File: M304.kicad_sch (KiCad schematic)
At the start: 89 parts, among them J1 LCD 2004, J2 Relay OUT, J3 iM920, J4 GPS, J5 Conn_01x02, P1 Digital, P10 CONN_01X01, P11 CONN_01X01, P12 CONN_01X01, P13 CONN_01X01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

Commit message: 大修正
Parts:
- removed JA15: Conn_01x03, Connector_JST:JST_XH_B3B-XH-A_1x03_P2.50mm_Vertical, symbol Connector_Generic:Conn_01x03
- added RV2: B10k, Potentiometer_THT:Potentiometer_Alps_RK09K_Single_Vertical, symbol Device:R_Potentiometer_MountingPin
- C1, C2: footprint (none) -> Capacitor_THT:C_Disc_D3.0mm_W2.0mm_P2.50mm
- C3: value 100u/35V -> 100u/25V; footprint (none) -> Capacitor_THT:CP_Radial_D5.0mm_P2.00mm
- J5: footprint (none) -> Connector_JST:JST_VH_B2P-VH_1x02_P3.96mm_Vertical
- R1, R2, R3, R4, R5, R6: footprint (none) -> Resistor_THT:R_Axial_DIN0207_L6.3mm_D2.5mm_P7.62mm_Horizontal
- RV1: value 10k -> B10k
- SW1, SW2, SW3, SW4, SW5: footprint (none) -> HOLLY:TVDT18-050
- U1: footprint Package_DIP:DIP-8_W7.62mm -> Package_DIP:DIP-8_W7.62mm_LongPads
- Y1: footprint (none) -> Crystal:Crystal_C26-LF_D2.1mm_L6.5mm_Horizontal
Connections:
- net +5V: now also RV1.3, RV2.3; no longer RV1.1
- net A15: now also RV2.2
- net GND: now also RV1.1, RV2.1, RV2.MP (MountPin); no longer RV1.3
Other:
- note added: "P-14827"

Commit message: PCB layout
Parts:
- removed JD32: Conn_01x01, Connector_Pin:Pin_D0.9mm_L10.0mm_W2.4mm_FlatFork, symbol Connector_Generic:Conn_01x01
- added SW6: SW_ENTER, HOLLY:TVDT18-050, symbol Switch:SW_SPST
- J1: footprint Connector_PinHeader_2.54mm:PinHeader_1x16_P2.54mm_Vertical -> Connector_PinSocket_2.54mm:PinSocket_1x16_P2.54mm_Vertical
- P2: footprint Socket_Arduino_Mega:Socket_Strip_Arduino_1x08 -> Connector_PinHeader_2.54mm:PinHeader_1x08_P2.54mm_Vertical
- renumbered SW6 to SW7
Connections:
- net 32: now also SW6.2 (B)
- net GND: now also SW6.1 (A)
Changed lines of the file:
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@@
     (stroke (width 0) (type default) (color 0 0 0 0))
   )
+  (wire (pts (xy 165.1 161.29) (xy 165.1 165.1))
+    (stroke (width 0) (type default) (color 0 0 0 0))
+  )
   (wire (pts (xy 30.48 124.46) (xy 36.83 124.46))
     (stroke (width 0) (type default) (color 0 0 0 0))
   )
+  (wire (pts (xy 167.64 176.53) (xy 167.64 179.07))
+    (stroke (width 0) (type default) (color 0 0 0 0))
+  )
   (wire (pts (xy 149.86 120.65) (xy 149.86 135.89))
     (stroke (width 0) (type default) (color 0 0 0 0))
@@
     (stroke (width 0) (type default) (color 0 0 0 0))
   )
+  (wire (pts (xy 167.64 165.1) (xy 167.64 166.37))
+    (stroke (width 0) (type default) (color 0 0 0 0))
+  )
   (wire (pts (xy 156.21 72.39) (xy 179.07 72.39))
     (stroke (width 0) (type solid) (color 0 0 0 0))
@@
     (stroke (width 0) (type default) (color 0 0 0 0))
   )
+  (wire (pts (xy 165.1 165.1) (xy 167.64 165.1))
+    (stroke (width 0) (type default) (color 0 0 0 0))
+  )
   (wire (pts (xy 39.37 127) (xy 39.37 138.43))
     (stroke (width 0) (type default) (color 0 0 0 0))
@@
     (stroke (width 0) (type default) (color 0 0 0 0))
   )
-  (wire (pts (xy 146.05 161.29) (xy 151.13 161.29))
-    (stroke (width 0) (type solid) (color 0 0 0 0))
-  )
   (wire (pts (xy 177.8 162.56) (xy 194.31 162.56))
     (stroke (width 0) (type default) (color 0 0 0 0))
@@
     (stroke (width 0) (type default) (color 0 0 0 0))
   )
+  (wire (pts (xy 146.05 161.29) (xy 165.1 161.29))
+    (stroke (width 0) (type default) (color 0 0 0 0))
+  )
   (wire (pts (xy 209.55 149.86) (xy 209.55 142.24))
     (stroke (width 0) (type default) (color 0 0 0 0))
@@
     (property "Reference" "P2" (id 0) (at 140.97 41.91 0))
     (property "Value" "Power" (id 1) (at 143.51 52.07 90))
-    (property "Footprint" "Socket_Arduino_Mega:Socket_Strip_Arduino_1x08" (id 2) (at 140.97 52.07 0)
+    (property "Footprint" "Connector_PinHeader_2.54mm:PinHeader_1x08_P2.54mm_Vertical" (id 2) (at 140.97 52.07 0)
       (effects (font (size 1.27 1.27)) hide)
     )
@@
       (effects (font (size 1.27 1.27)) (justify left))
     )
-    (property "Footprint" "Connector_PinHeader_2.54mm:PinHeader_1x16_P2.54mm_Vertical" (id 2) (at 224.79 142.24 0)
+    (property "Footprint" "Connector_PinSocket_2.54mm:PinSocket_1x16_P2.54mm_Vertical" (id 2) (at 224.79 142.24 0)
       (effects (font (size 1.27 1.27)) hide)
     )
@@
     (pin "3")
   )
+  (symbol (lib_id "power:GND") (at 167.64 179.07 0) (unit 1)
+    (in_bom yes) (on_board yes)
+    (property "Reference" "#PWR0138" (id 0) (at 167.64 185.42 0)
+      (effects (font (size 1.27 1.27)) hide)
+    )
+    (property "Value" "GND" (id 1) (at 167.64 184.15 90)
+      (effects (font (size 1 1)))
+    )
+    (property "Footprint" "" (id 2) (at 167.64 179.07 0))
+    (property "Datasheet" "" (id 3) (at 167.64 179.07 0))
+    (pin "1")
+  )
   (symbol (lib_id "power:GND") (at 269.24 50.8 0) (unit 1)
     (in_bom yes) (on_board yes)
@@
   (symbol (lib_id "Switch:SW_SPST") (at 193.802 82.55 0) (mirror y) (unit 1)
     (in_bom yes) (on_board yes)
-    (property "Reference" "SW6" (id 0) (at 189.992 81.28 0)
+    (property "Reference" "SW7" (id 0) (at 189.992 81.28 0)
       (effects (font (size 1 1)))
     )
@@
     (pin "2")
   )
-  (symbol (lib_id "Connector_Generic:Conn_01x01") (at 156.21 161.29 0) (unit 1)
-    (in_bom yes) (on_board yes)
-    (property "Reference" "JD32" (id 0) (at 158.75 161.29 0)
-      (effects (font (size 1.27 1.27)) (justify left))
-    )
-    (property "Value" "Conn_01x01" (id 1) (at 158.242 162.9922 0)
-      (effects (font (size 1.27 1.27)) (justify left) hide)
-    )
-    (property "Footprint" "Connector_Pin:Pin_D0.9mm_L10.0mm_W2.4mm_FlatFork" (id 2) (at 156.21 161.29 0)
-      (effects (font (size 1.27 1.27)) hide)
-    )
-    (property "Datasheet" "~" (id 3) (at 156.21 161.29 0)
-      (effects (font (size 1.27 1.27)) hide)
-    )
-    (pin "1")
-  )
   (symbol (lib_id "Connector_Generic:Conn_01x02") (at 260.35 36.83 0) (unit 1)
     (in_bom yes) (on_board yes)
@@
     (pin "5")
   )
+  (symbol (lib_id "Switch:SW_SPST") (at 167.64 171.45 270) (mirror x) (unit 1)
+    (in_bom yes) (on_board yes)
+    (property "Reference" "SW6" (id 0) (at 165.1 171.45 90)
+      (effects (font (size 1 1)))
+    )
+    (property "Value" "SW_ENTER" (id 1) (at 172.72 172.72 90)
+      (effects (font (size 1 1)))
+    )
+    (property "Footprint" "HOLLY:TVDT18-050" (id 2) (at 167.64 171.45 0)
+      (effects (font (size 1.27 1.27)) hide)
+    )
+    (property "Datasheet" "~" (id 3) (at 167.64 171.45 0)
+      (effects (font (size 1.27 1.27)) hide)
+    )
+    (pin "1")
+    (pin "2")
+  )
   (symbol (lib_id "power:GND") (at 82.55 35.56 0) (unit 1)
     (in_bom yes) (on_board yes)
@@
       (reference "#PWR0137") (unit 1) (value "GND") (footprint "")
     )
+    (path "/3a7afde4-db0a-4309-bece-1305421c4024"
+      (reference "#PWR0138") (unit 1) (value "GND") (footprint "")
+    )
     (path "/7629fb6d-20db-4e52-aca9-1faafbccf85c"
       (reference "BT1") (unit 1) (value "CR2032") (footprint "")
@@
     )
     (path "/2812c426-eaaa-40f0-875f-9c01c02e0a76"
-      (reference "J1") (unit 1) (value "LCD 2004") (footprint "Connector_PinHeader_2.54mm:PinHeader_1x16_P2.54mm_Vertical")
+      (reference "J1") (unit 1) (value "LCD 2004") (footprint "Connector_PinSocket_2.54mm:PinSocket_1x16_P2.54mm_Vertical")
     )
     (path "/cf4a0d7b-49d0-4fab-a66e-8cf646496452"
@@
       (reference "JD31") (unit 1) (value "Conn_01x01") (footprint "Connector_Pin:Pin_D0.9mm_L10.0mm_W2.4mm_FlatFork")
     )
-    (path "/9eb5f420-8ac2-4cff-9412-80ef6b7747c6"
-      (reference "JD32") (unit 1) (value "Conn_01x01") (footprint "Connector_Pin:Pin_D0.9mm_L10.0mm_W2.4mm_FlatFork")
-    )
     (path "/b0e37c59-828f-45f4-9524-3ceeeb2c5150"
       (reference "JD48") (unit 1) (value "Conn_01x01") (footprint "Connector_Pin:Pin_D0.9mm_L10.0mm_W2.4mm_FlatFork")
@@
     )
     (path "/00000000-0000-0000-0000-000056d71773"
-      (reference "P2") (unit 1) (value "Power") (footprint "Socket_Arduino_Mega:Socket_Strip_Arduino_1x08")
+      (reference "P2") (unit 1) (value "Power") (footprint "Connector_PinHeader_2.54mm:PinHeader_1x08_P2.54mm_Vertical")
     )
     (path "/00000000-0000-0000-0000-000056d72f1c"
@@
       (reference "SW5") (unit 1) (value "SW_D") (footprint "HOLLY:TVDT18-050")
     )
+    (path "/eab964a3-3b27-437e-9f6c-be163cd40f3e"
+      (reference "SW6") (unit 1) (value "SW_ENTER") (footprint "HOLLY:TVDT18-050")
+    )
     (path "/70315b01-1acb-4620-a09c-cc62e59d80b5"
-      (reference "SW6") (unit 1) (value "SAFEMODE") (footprint "")
+      (reference "SW7") (unit 1) (value "SAFEMODE") (footprint "")
     )
     (path "/2da95ce6-0997-43ec-959b-0f1144d39cac"

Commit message: Arduino MEGA pin direction change
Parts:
- P1: footprint Socket_Arduino_Mega:Socket_Strip_Arduino_2x18 -> Connector_PinHeader_2.54mm:PinHeader_2x18_P2.54mm_Vertical
- P3, P4, P6, P7: footprint Socket_Arduino_Mega:Socket_Strip_Arduino_1x08 -> Connector_PinHeader_2.54mm:PinHeader_1x08_P2.54mm_Vertical
- P5: footprint Socket_Arduino_Mega:Socket_Strip_Arduino_1x10 -> Connector_PinHeader_2.54mm:PinHeader_1x10_P2.54mm_Vertical
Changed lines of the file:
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@@
     (property "Reference" "P5" (id 0) (at 151.13 36.83 0))
     (property "Value" "PWM" (id 1) (at 148.59 49.53 90))
-    (property "Footprint" "Socket_Arduino_Mega:Socket_Strip_Arduino_1x10" (id 2) (at 151.13 49.53 0)
+    (property "Footprint" "Connector_PinHeader_2.54mm:PinHeader_1x10_P2.54mm_Vertical" (id 2) (at 151.13 49.53 0)
       (effects (font (size 1.27 1.27)) hide)
     )
@@
     (property "Reference" "P3" (id 0) (at 140.97 69.85 0))
     (property "Value" "Analog" (id 1) (at 143.51 80.01 90))
-    (property "Footprint" "Socket_Arduino_Mega:Socket_Strip_Arduino_1x08" (id 2) (at 140.97 80.01 0)
+    (property "Footprint" "Connector_PinHeader_2.54mm:PinHeader_1x08_P2.54mm_Vertical" (id 2) (at 140.97 80.01 0)
       (effects (font (size 1.27 1.27)) hide)
     )
@@
     (property "Reference" "P6" (id 0) (at 151.13 69.85 0))
     (property "Value" "PWM" (id 1) (at 148.59 80.01 90))
-    (property "Footprint" "Socket_Arduino_Mega:Socket_Strip_Arduino_1x08" (id 2) (at 151.13 80.01 0)
+    (property "Footprint" "Connector_PinHeader_2.54mm:PinHeader_1x08_P2.54mm_Vertical" (id 2) (at 151.13 80.01 0)
       (effects (font (size 1.27 1.27)) hide)
     )
@@
     (property "Reference" "P4" (id 0) (at 140.97 93.98 0))
     (property "Value" "Analog" (id 1) (at 143.51 104.14 90))
-    (property "Footprint" "Socket_Arduino_Mega:Socket_Strip_Arduino_1x08" (id 2) (at 140.97 104.14 0)
+    (property "Footprint" "Connector_PinHeader_2.54mm:PinHeader_1x08_P2.54mm_Vertical" (id 2) (at 140.97 104.14 0)
       (effects (font (size 1.27 1.27)) hide)
     )
@@
     (property "Reference" "P7" (id 0) (at 151.13 93.98 0))
     (property "Value" "Communication" (id 1) (at 148.59 104.14 90))
-    (property "Footprint" "Socket_Arduino_Mega:Socket_Strip_Arduino_1x08" (id 2) (at 151.13 104.14 0)
+    (property "Footprint" "Connector_PinHeader_2.54mm:PinHeader_1x08_P2.54mm_Vertical" (id 2) (at 151.13 104.14 0)
       (effects (font (size 1.27 1.27)) hide)
     )
@@
     (property "Reference" "P1" (id 0) (at 140.97 129.54 0))
     (property "Value" "Digital" (id 1) (at 140.97 153.67 90))
-    (property "Footprint" "Socket_Arduino_Mega:Socket_Strip_Arduino_2x18" (id 2) (at 140.97 180.34 0)
+    (property "Footprint" "Connector_PinHeader_2.54mm:PinHeader_2x18_P2.54mm_Vertical" (id 2) (at 140.97 180.34 0)
       (effects (font (size 1.27 1.27)) hide)
     )
@@
     )
     (path "/00000000-0000-0000-0000-000056d743b5"
-      (reference "P1") (unit 1) (value "Digital") (footprint "Socket_Arduino_Mega:Socket_Strip_Arduino_2x18")
+      (reference "P1") (unit 1) (value "Digital") (footprint "Connector_PinHeader_2.54mm:PinHeader_2x18_P2.54mm_Vertical")
     )
     (path "/00000000-0000-0000-0000-000056d71773"
@@
     )
     (path "/00000000-0000-0000-0000-000056d72f1c"
-      (reference "P3") (unit 1) (value "Analog") (footprint "Socket_Arduino_Mega:Socket_Strip_Arduino_1x08")
+      (reference "P3") (unit 1) (value "Analog") (footprint "Connector_PinHeader_2.54mm:PinHeader_1x08_P2.54mm_Vertical")
     )
     (path "/00000000-0000-0000-0000-000056d73a0e"
-      (reference "P4") (unit 1) (value "Analog") (footprint "Socket_Arduino_Mega:Socket_Strip_Arduino_1x08")
+      (reference "P4") (unit 1) (value "Analog") (footprint "Connector_PinHeader_2.54mm:PinHeader_1x08_P2.54mm_Vertical")
     )
     (path "/00000000-0000-0000-0000-000056d72368"
-      (reference "P5") (unit 1) (value "PWM") (footprint "Socket_Arduino_Mega:Socket_Strip_Arduino_1x10")
+      (reference "P5") (unit 1) (value "PWM") (footprint "Connector_PinHeader_2.54mm:PinHeader_1x10_P2.54mm_Vertical")
     )
     (path "/00000000-0000-0000-0000-000056d734d0"
-      (reference "P6") (unit 1) (value "PWM") (footprint "Socket_Arduino_Mega:Socket_Strip_Arduino_1x08")
+      (reference "P6") (unit 1) (value "PWM") (footprint "Connector_PinHeader_2.54mm:PinHeader_1x08_P2.54mm_Vertical")
     )
     (path "/00000000-0000-0000-0000-000056d73f2c"
-      (reference "P7") (unit 1) (value "Communication") (footprint "Socket_Arduino_Mega:Socket_Strip_Arduino_1x08")
+      (reference "P7") (unit 1) (value "Communication") (footprint "Connector_PinHeader_2.54mm:PinHeader_1x08_P2.54mm_Vertical")
     )
     (path "/00000000-0000-0000-0000-000056d70b71"

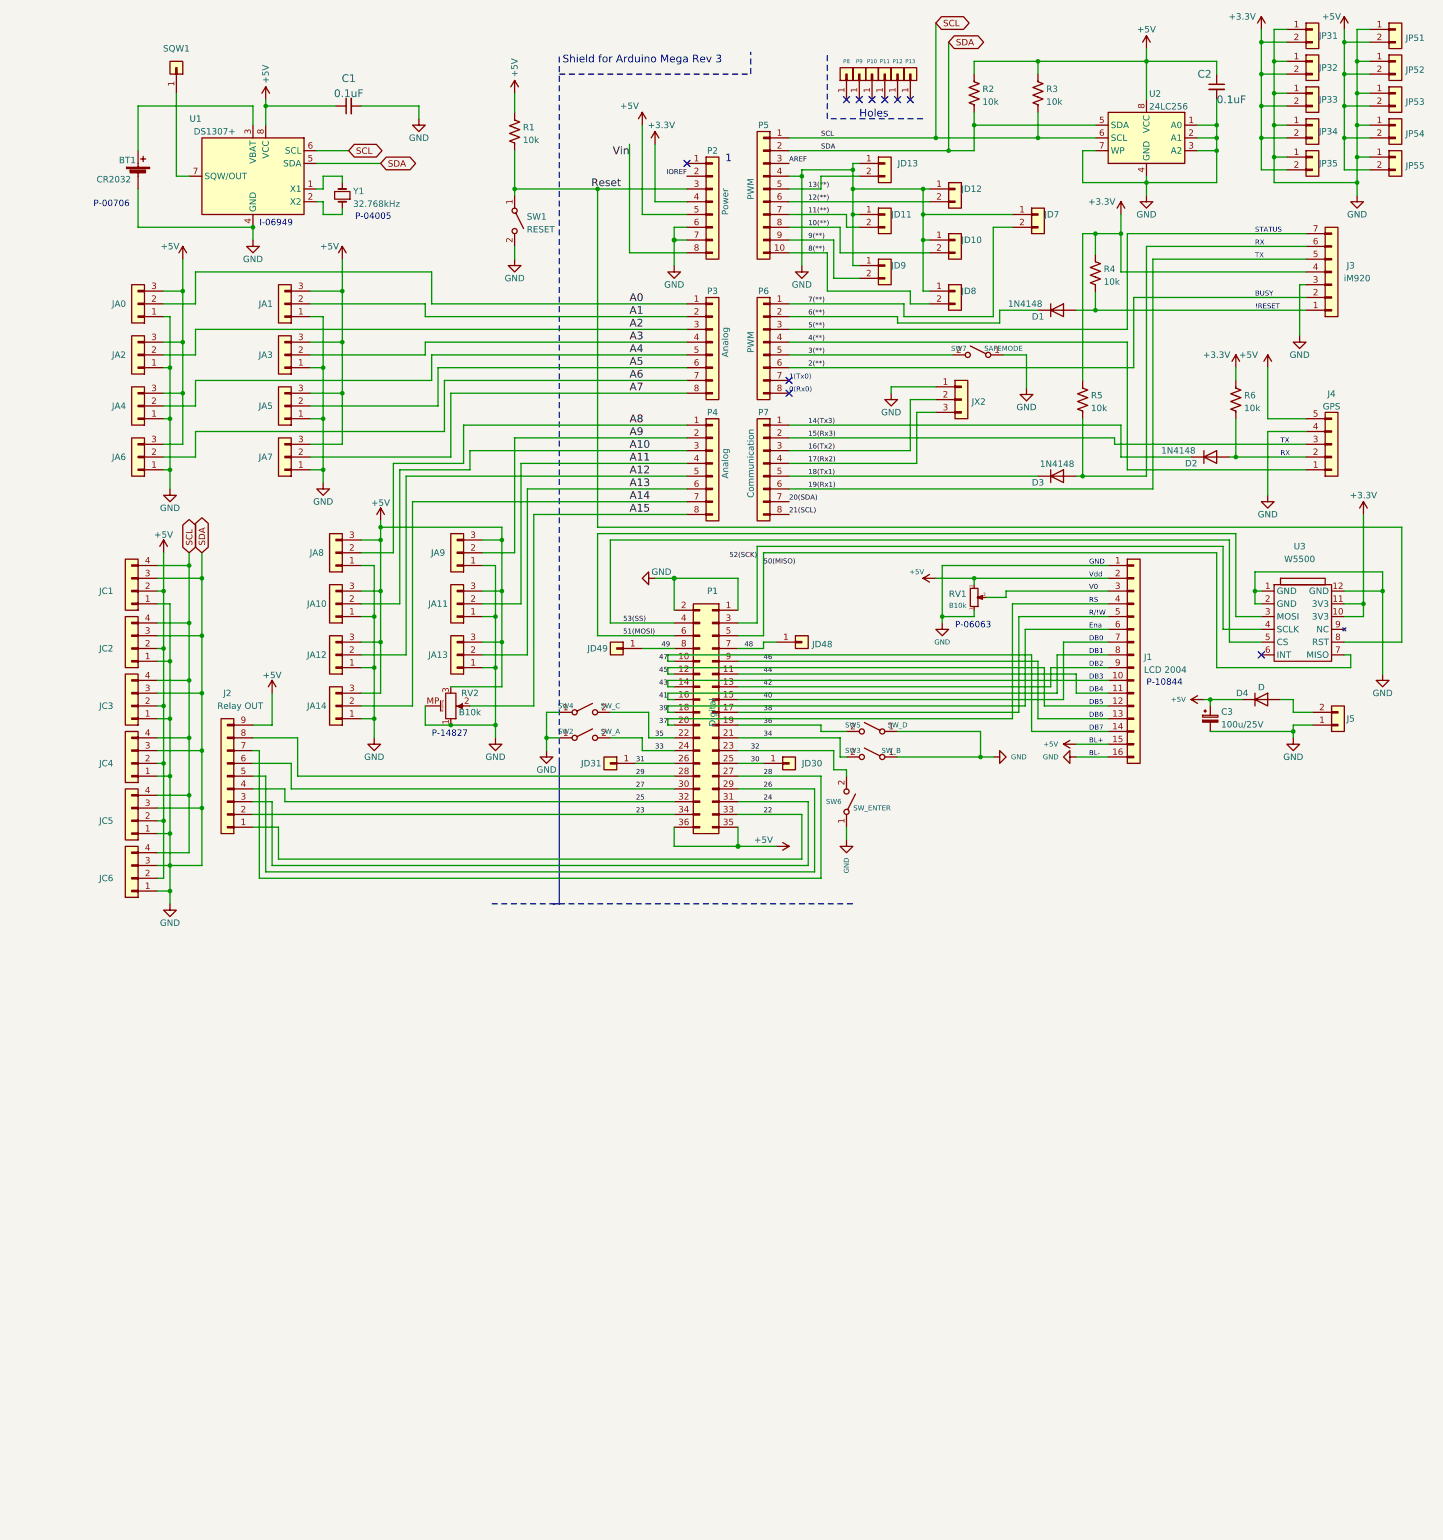
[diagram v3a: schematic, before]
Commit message: Photo coupler append
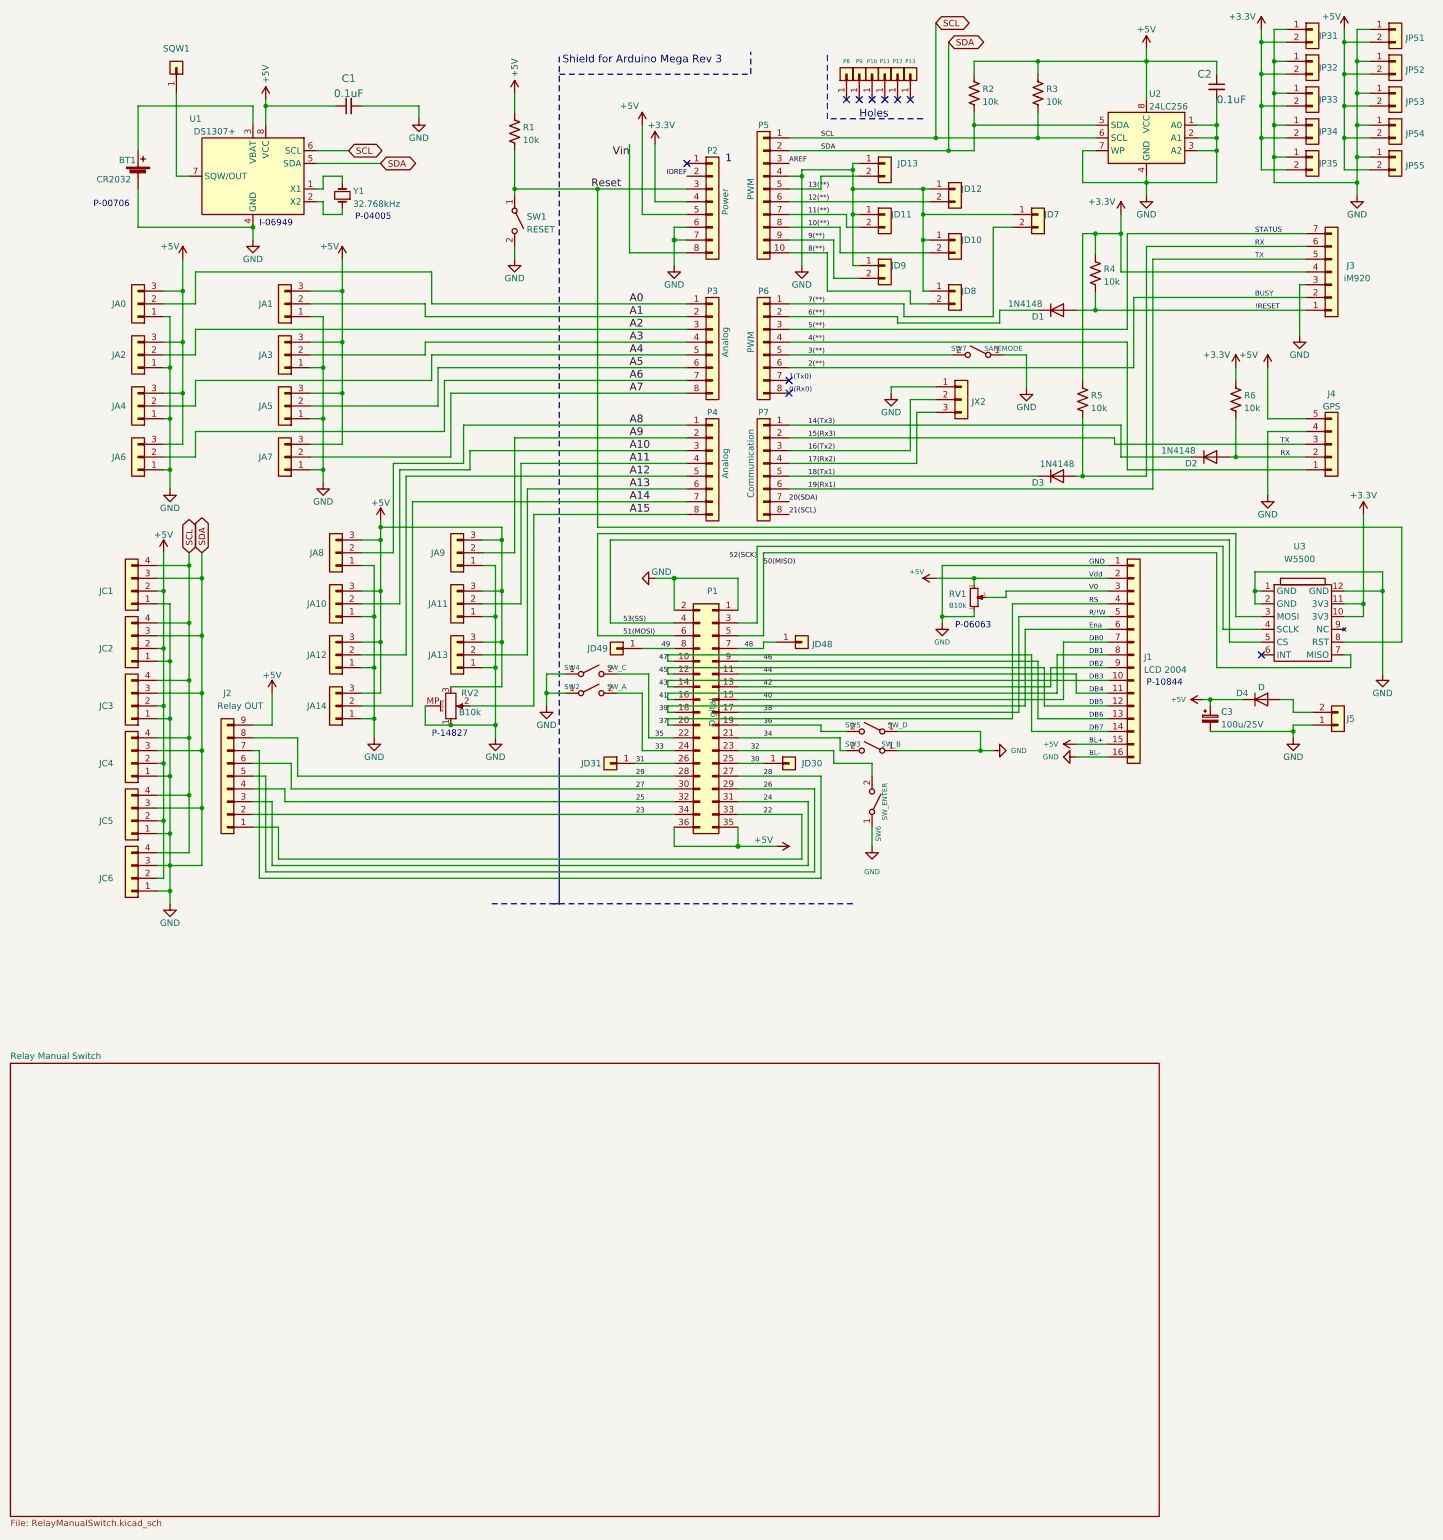
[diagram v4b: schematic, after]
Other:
- added sheet Relay Manual Switch (RelayManualSwitch.kicad_sch)
- moved on the sheet: SW2, SW3, SW4, SW6
